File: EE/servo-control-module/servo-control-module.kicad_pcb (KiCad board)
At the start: 2 copper layers, 27.8 x 35.4 mm, 4 parts, among them J1 SERVO, J2 USB, U1 ATtiny85-20P

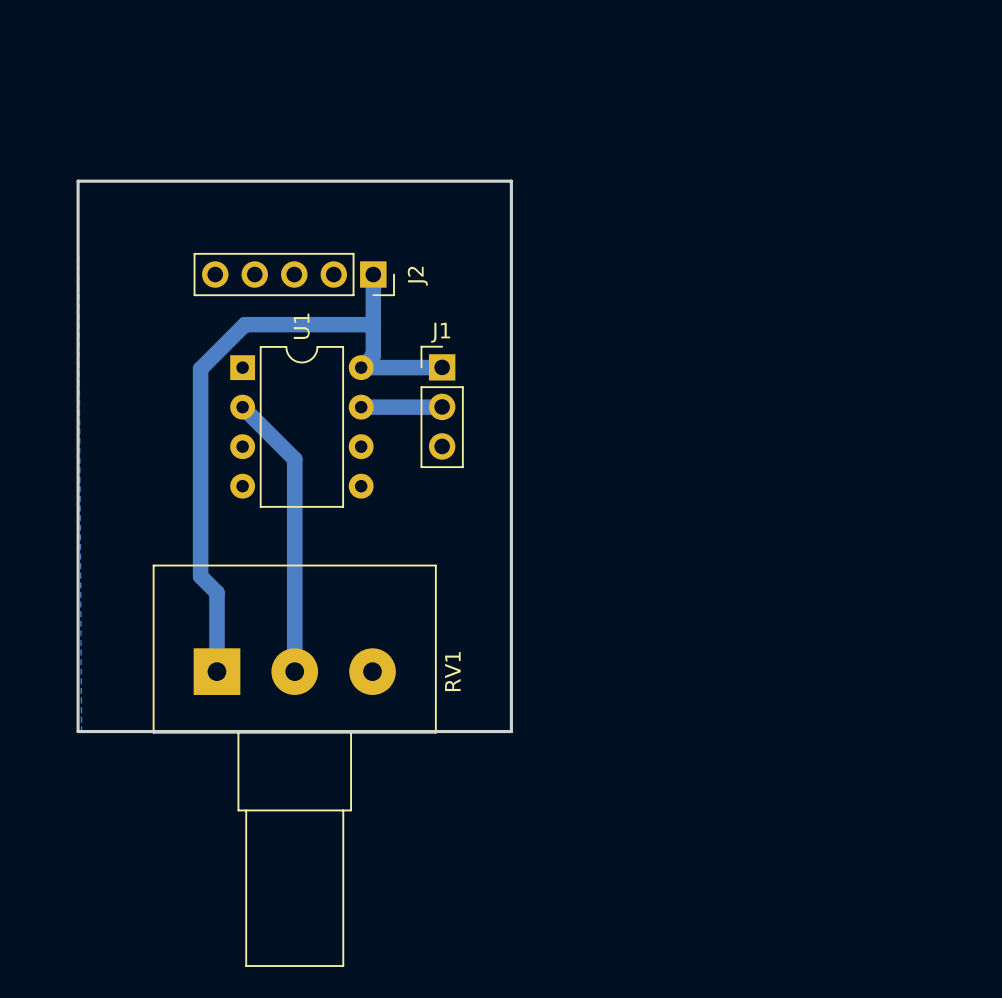
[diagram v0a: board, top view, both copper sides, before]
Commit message: Added footprint and 3D model for USB breakout adapter.
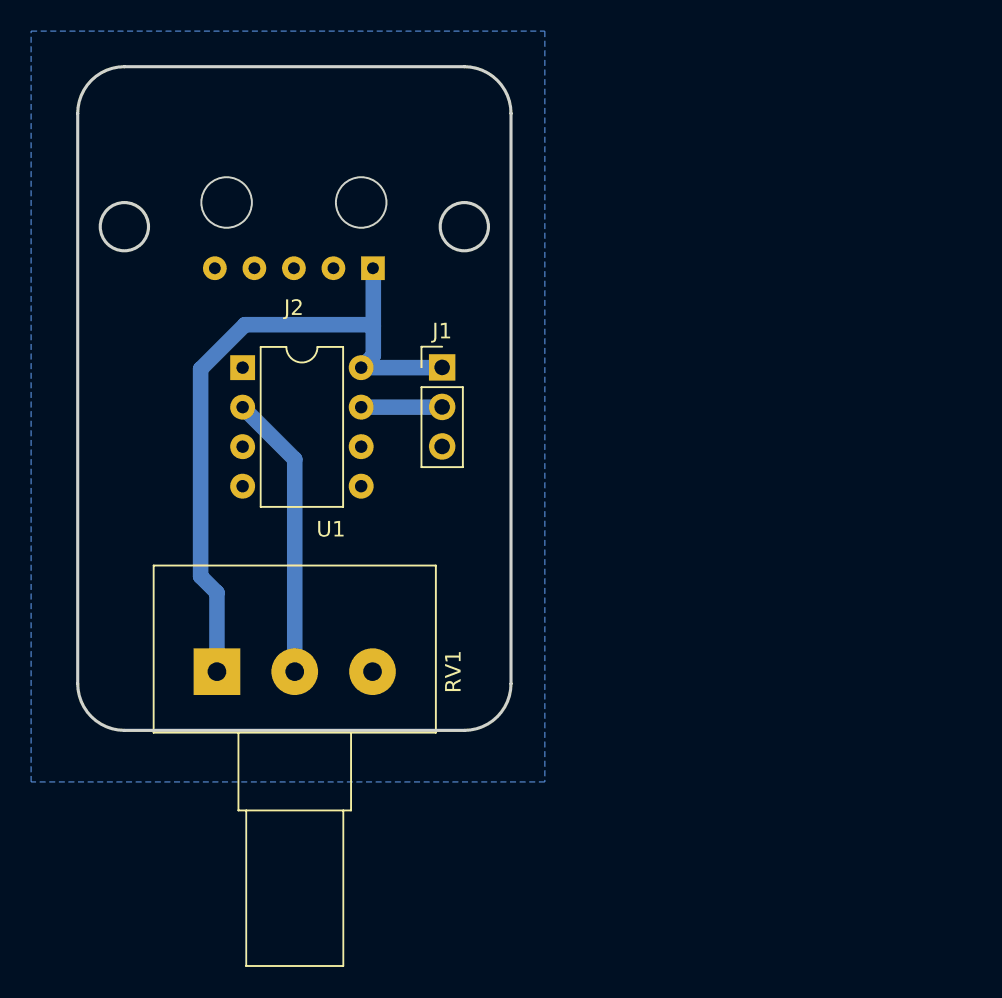
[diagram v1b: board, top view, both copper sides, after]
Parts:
- J2: footprint Connector_PinSocket_2.54mm:PinSocket_1x05_P2.54mm_Vertical -> Library:USB-micro-breakout
- RV1: footprint Potentiometer_THT:Potentiometer_Alps_RK163_Single_Horizontal -> Library:Potentiometer_Amazon_Single_Horizontal
- moved J2 5.12 mm to (110.9, 83.8), turned to 180 degrees
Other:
- board size 27.8 x 35.4 mm -> 27.9 x 42.7 mm

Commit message: Updated to KiCad v8
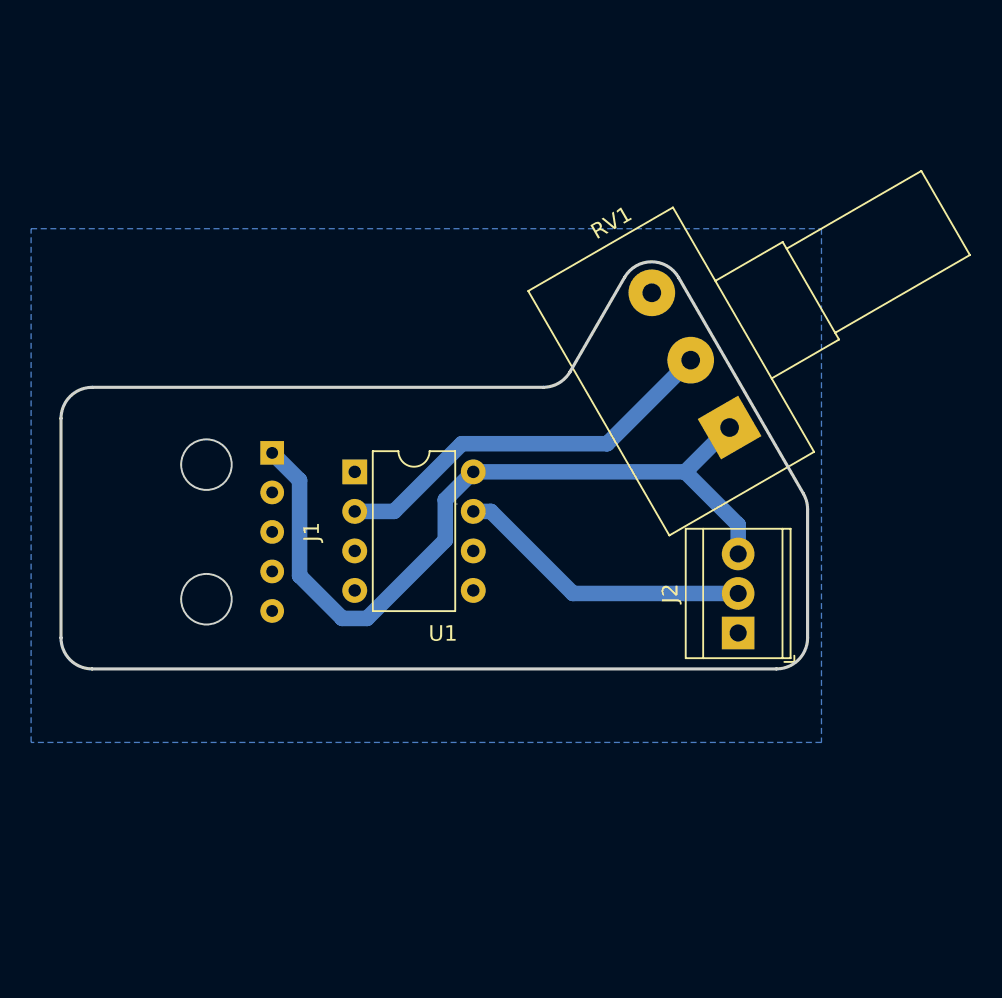
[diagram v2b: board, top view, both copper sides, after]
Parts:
- removed the J1 at (120.4, 90.2)
- added J2: SERVO, TerminalBlock_TE-Connectivity:TerminalBlock_TE_282834-3_1x03_P2.54mm_Horizontal, F.Cu at (139.4, 107.3)
- moved RV1 36.5 mm to (138.9, 94.1), turned to -150 degrees
- moved J1 17.0 mm to (109.5, 100.8), turned to -90 degrees
- moved U1 9.84 mm to (114.8, 96.9)
- renumbered J2 to J1
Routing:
- net SERVO: track 5.06 -> 19.2 mm
- net V-POT: track 18.4 -> 25.6 mm
- net +5V: track 43.7 -> 50.7 mm
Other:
- board size 27.9 x 42.7 mm -> 48 x 26.2 mm
- board text added: "ATTiny85"
- board text added: "DESIGNS"
- board text added: "DLH"
- board text added: "U1"
